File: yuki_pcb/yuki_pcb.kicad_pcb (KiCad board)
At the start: 2 copper layers, 141.6 x 98 mm, 31 parts, among them J1 TRRS, K00 KEYSW, K01 KEYSW, K02 KEYSW, K03 KEYSW, K04 KEYSW, K05 KEYSW, K10 KEYSW, K11 KEYSW, K12 KEYSW, K13 KEYSW, K14 KEYSW, K15 KEYSW, K20 KEYSW, K21 KEYSW, K22 KEYSW, K23 KEYSW, K24 KEYSW, K25 KEYSW, K30 KEYSW, K31 KEYSW, K32 KEYSW, K33 KEYSW, U1 YAAJ_WeAct_BlackPill_Part_Like

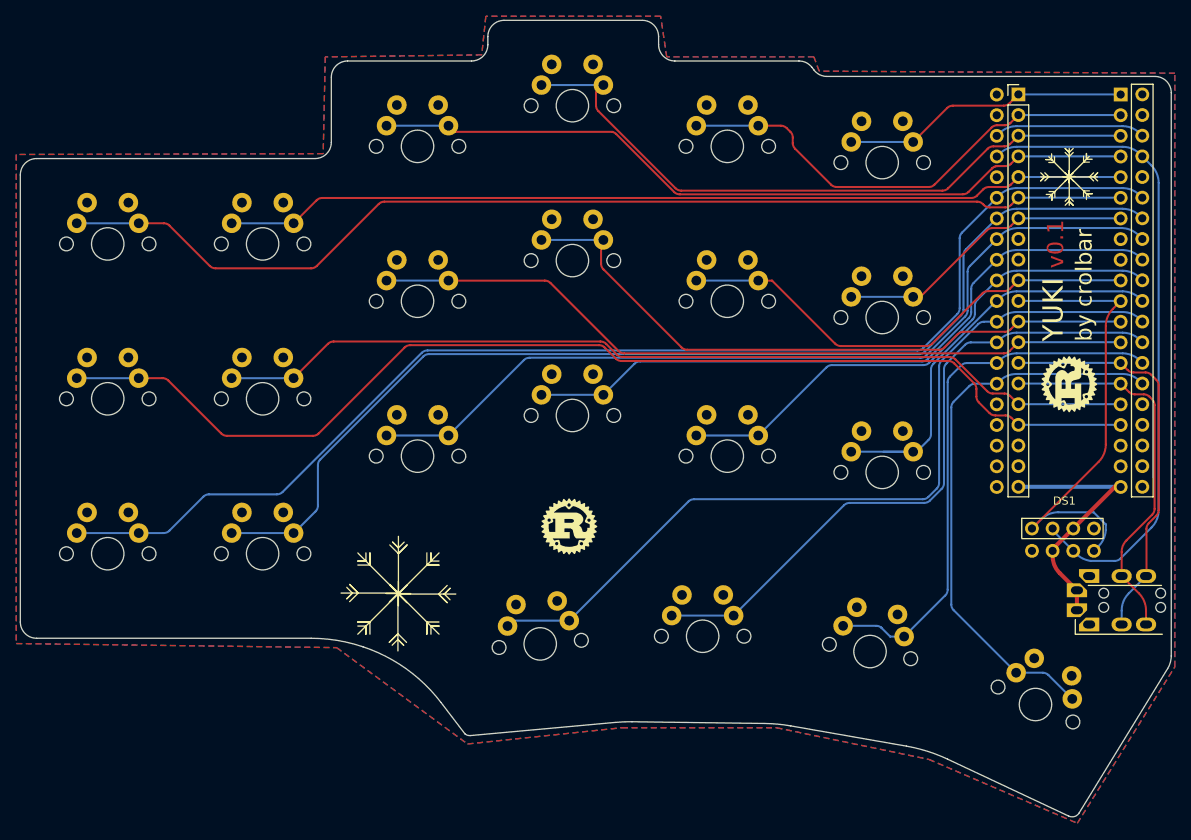
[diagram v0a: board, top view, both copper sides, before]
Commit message: choc footprint + half tracks done
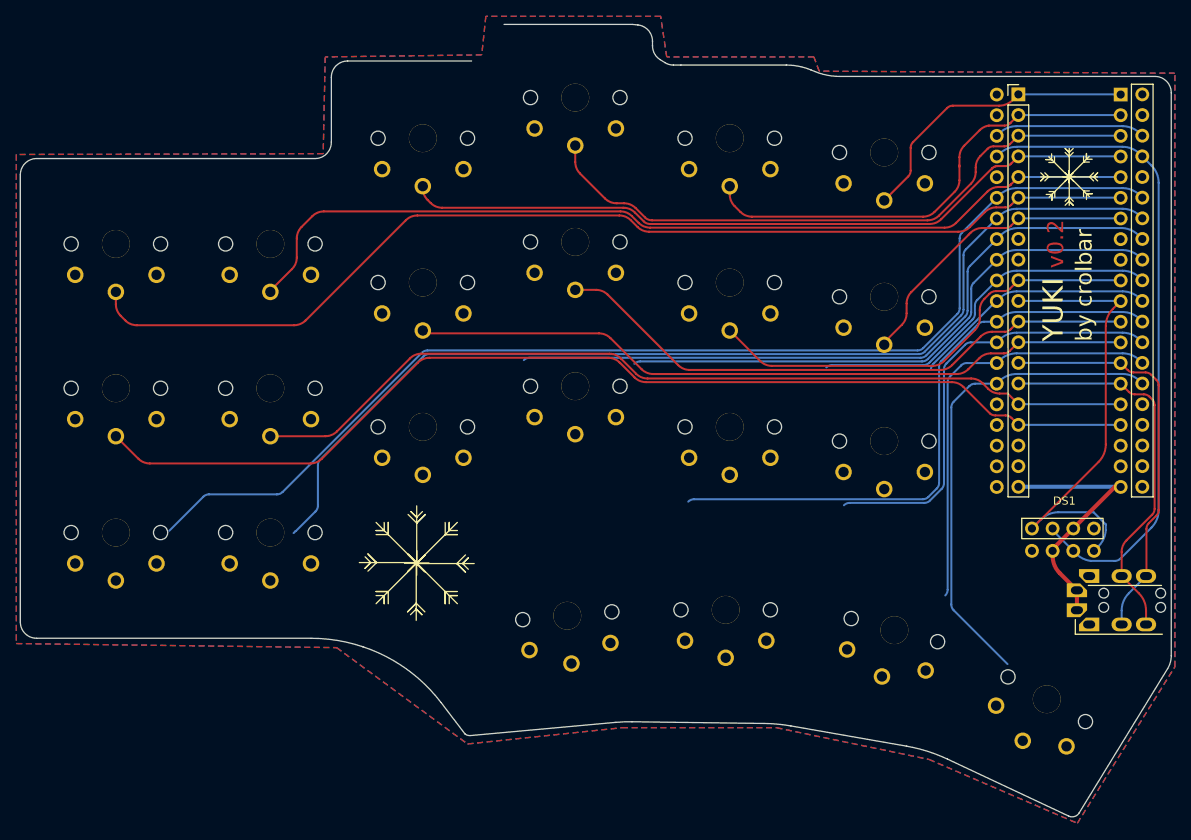
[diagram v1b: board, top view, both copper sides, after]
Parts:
- removed G*** (x3): LOGO, YUKI:RUST_GEAR
- K00, K01, K02, K03, K04, K05, K10, K11, K12, K13, K14, K15, K20, K21, K22, K23, K24, K25, K30, K31, K32, K33: footprint YUKI:CherryMX_rev -> YUKI:Kailh_Choc_PG1350_rev
- moved K30 4.81 mm to (125.3, 115.7)
- moved REF** 4.37 mm to (106.8, 109.2) (x2)
- moved K31 4.31 mm to (144.8, 115.0)
- moved K32 3.99 mm to (165.5, 117.5), turned to -15 degrees
- moved K25 3.86 mm to (164.2, 94.2)
- moved K22 3.66 mm to (107.5, 92.5)
- moved K23 3.62 mm to (126.2, 87.5)
- moved K24 3.61 mm to (145.2, 92.5)
- moved K20 2.79 mm to (69.8, 105.5)
- moved K21 2.77 mm to (88.8, 105.5)
- moved K15 2.56 mm to (164.2, 76.5)
- moved K12 2.39 mm to (107.5, 74.8)
- moved K13 2.33 mm to (126.2, 69.8)
- moved K14 2.32 mm to (145.2, 74.8)
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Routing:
- net /k30: track 103.7 -> 75.1 mm
- net /k31: track 81.7 -> 54.9 mm
- net /k25: track 53.6 -> 31.2 mm
- net /k22: track 107.7 -> 87.0 mm
- net /k24: track 65.0 -> 45.5 mm
- net /k32: track 68.2 -> 52.8 mm
- net /k23: track 84.3 -> 71.2 mm
- net /k20: track 155.3 -> 143.3 mm
- net /k33: track 70.5 -> 60.8 mm
- net /k21: track 137.0 -> 129.4 mm
- net /k10: track 140.5 -> 133.1 mm
- net /k13: track 80.3 -> 73.2 mm
- net /k12: track 94.4 -> 89.2 mm
- net /k03: track 82.2 -> 77.5 mm
- net /k02: track 95.5 -> 91.3 mm
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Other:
- board size 141.6 x 98 mm -> 141.6 x 97.5 mm
- board text added: "v0.2"
- board text removed: "v0.1"

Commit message: back tracks done
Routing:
- net /k22: track 87.0 -> 114.4 mm
- net /k30: track 75.1 -> 100.3 mm
- net /k31: track 54.9 -> 76.5 mm
- net /k24: track 45.5 -> 64.3 mm
- net /k25: track 31.2 -> 48.2 mm
- net /k21: track 129.4 -> 146.2 mm
- net /k20: track 143.3 -> 156.7 mm
- net /k23: track 71.2 -> 83.5 mm
- net /k32: track 52.8 -> 64.7 mm
- net /k33: track 60.8 -> 70.8 mm
- net /k01: track 113.8 -> 113.3 mm
